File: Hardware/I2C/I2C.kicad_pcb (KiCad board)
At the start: 2 copper layers, 39.4 x 29.2 mm, 5 parts, among them P1 DIL16, P2 CONN_01X04

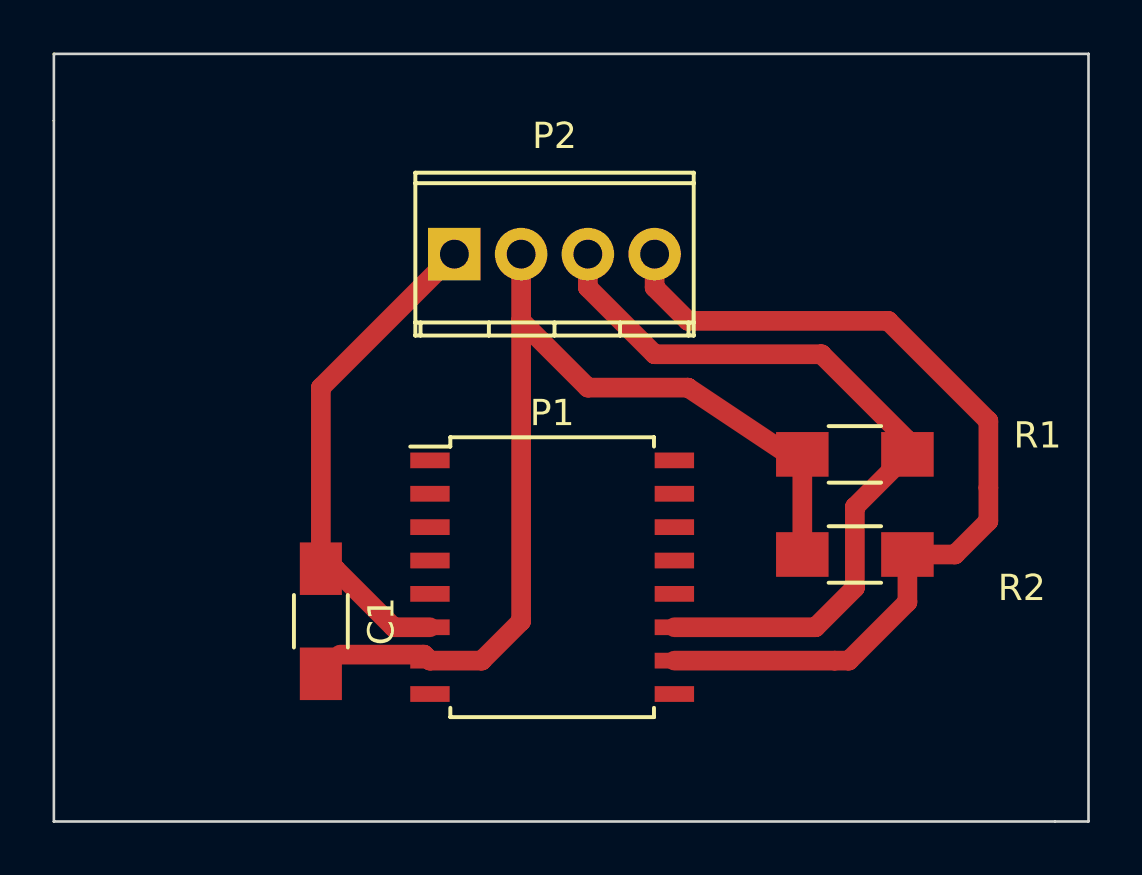
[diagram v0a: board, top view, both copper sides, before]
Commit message: updated I2C design, added various exports used in testing with cnc machine
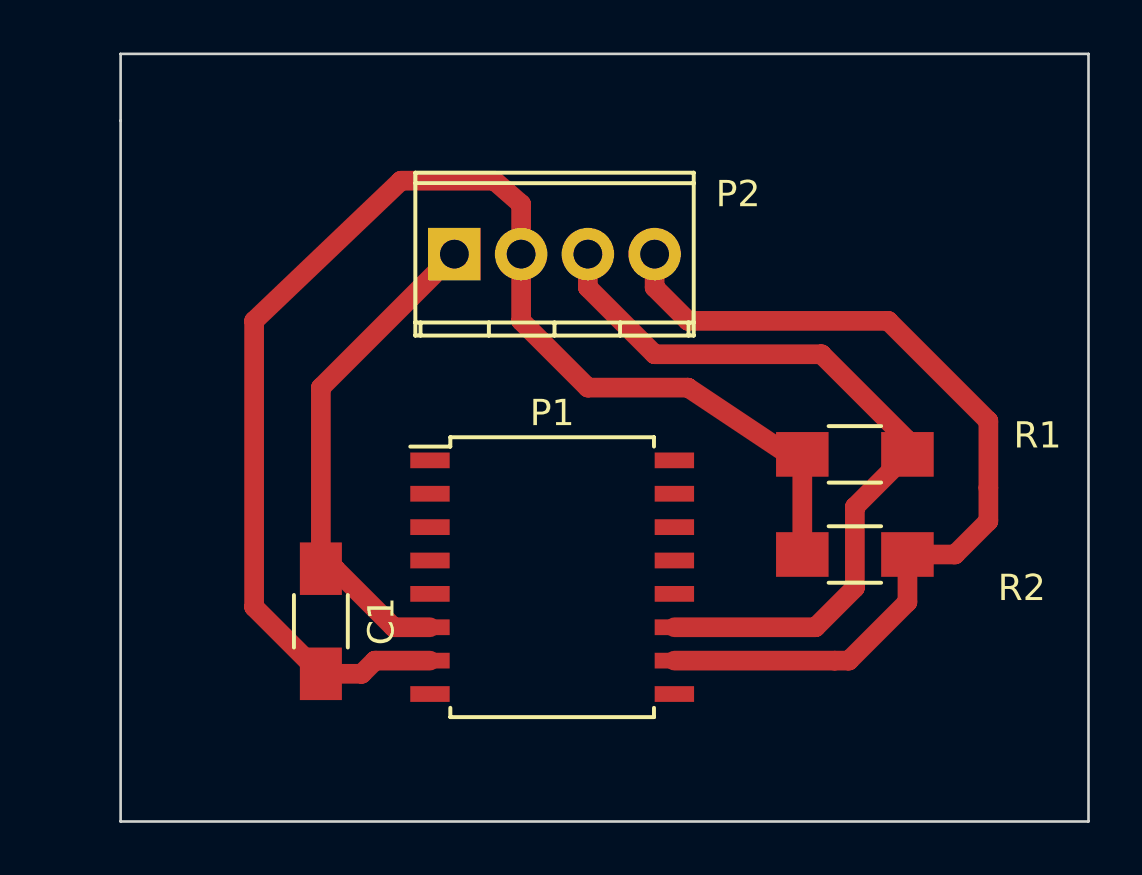
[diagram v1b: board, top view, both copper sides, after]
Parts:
- P1: value DIL16 -> SM9541
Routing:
- net Net-(C1-Pad2): track 37.9 -> 52.2 mm
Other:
- board size 39.4 x 29.2 mm -> 36.8 x 29.2 mm
- board text added: "GND Vs CLK DATA"
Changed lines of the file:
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@@
     (links 10)
     (no_connects 0)
-    (area 129.489999 85.039999 169.063198 114.350001)
+    (area 132.029999 85.039999 169.063198 114.350001)
     (thickness 1.6)
     (drawings 10)
-    (tracks 37)
+    (tracks 41)
     (zones 0)
     (modules 5)
@@
   )
   (setup
-    (last_trace_width 0.75)
+    (last_trace_width 0.25)
     (user_trace_width 0.75)
     (trace_clearance 0.2)
@@
     (pad_to_mask_clearance 0)
     (aux_axis_origin 0 0)
-    (visible_elements FFFFFF7F)
+    (visible_elements 7FFFFFFF)
     (pcbplotparams
-      (layerselection 0x00030_80000001)
+      (layerselection 0x00000_80000000)
       (usegerberextensions false)
       (excludeedgelayer true)
@@
       (padsonsilk false)
       (subtractmaskfromsilk false)
-      (outputformat 1)
+      (outputformat 5)
       (mirror false)
-      (drillshape 1)
+      (drillshape 0)
       (scaleselection 1)
       (outputdirectory ""))
@@
       (effects (font (size 1 1) (thickness 0.15)))
     )
-    (fp_text value DIL16 (at 0 6.25) (layer F.Fab)
+    (fp_text value SM9541 (at 0 6.25) (layer F.Fab)
       (effects (font (size 1 1) (thickness 0.15)))
     )
@@
     (at 144.78 92.71)
     (descr "4-way 2.54mm pitch terminal block, Phoenix MPT series")
-    (fp_text reference P2 (at 3.81 -4.50088) (layer F.SilkS)
+    (fp_text reference P2 (at 10.795 -2.286) (layer F.SilkS)
       (effects (font (size 1 1) (thickness 0.15)))
     )
@@
     )
   )
-  (gr_line (start 168.91 85.09) (end 129.54 85.09) (angle 90) (layer Edge.Cuts) (width 0.1))
-  (gr_line (start 168.91 114.3) (end 167.64 114.3) (angle 90) (layer Edge.Cuts) (width 0.1))
-  (gr_line (start 167.64 114.3) (end 129.54 114.3) (angle 90) (layer Edge.Cuts) (width 0.1))
-  (target plus (at 133.35 88.9) (size 5) (width 0.1) (layer Edge.Cuts))
+  (gr_line (start 132.08 85.09) (end 168.91 85.09) (angle 90) (layer Edge.Cuts) (width 0.1))
+  (gr_line (start 168.91 114.3) (end 132.08 114.3) (angle 90) (layer Edge.Cuts) (width 0.1))
+  (gr_text "GND Vs CLK DATA" (at 148.7805 88.519) (layer F.Mask)
+    (effects (font (size 1 1) (thickness 0.1)))
+  )
+  (target plus (at 135.636 88.9) (size 5) (width 0.1) (layer Edge.Cuts))
   (target plus (at 165.1 110.49) (size 5) (width 0.1) (layer Edge.Cuts))
   (target plus (at 165.1 88.9) (size 5) (width 0.1) (layer Edge.Cuts))
-  (target plus (at 133.35 110.49) (size 5) (width 0.1) (layer Edge.Cuts))
-  (gr_line (start 129.54 85.09) (end 129.54 87.63) (angle 90) (layer Edge.Cuts) (width 0.1))
+  (target plus (at 135.636 110.236) (size 5) (width 0.1) (layer Edge.Cuts))
+  (gr_line (start 132.08 85.09) (end 132.08 87.63) (angle 90) (layer Edge.Cuts) (width 0.1))
   (gr_line (start 168.91 114.3) (end 168.91 85.09) (angle 90) (layer Edge.Cuts) (width 0.1))
-  (gr_line (start 129.54 87.63) (end 129.54 114.3) (angle 90) (layer Edge.Cuts) (width 0.1))
+  (gr_line (start 132.08 87.63) (end 132.08 114.3) (angle 90) (layer Edge.Cuts) (width 0.1))
   (segment (start 144.78 92.71) (end 139.7 97.79) (width 0.75) (layer F.Cu) (net 1))
   (segment (start 139.7 97.79) (end 139.7 104.68) (width 0.75) (layer F.Cu) (net 1))
@@
   (segment (start 140.24 104.68) (end 142.4686 106.9086) (width 0.75) (layer F.Cu) (net 1))
   (segment (start 142.4686 106.9086) (end 143.8511 106.9086) (width 0.75) (layer F.Cu) (net 1))
-  (segment (start 143.8511 108.1786) (end 145.8214 108.1786) (width 0.75) (layer F.Cu) (net 2))
-  (segment (start 147.32 106.68) (end 147.32 95.25) (width 0.75) (layer F.Cu) (net 2))
-  (segment (start 145.8214 108.1786) (end 147.32 106.68) (width 0.75) (layer F.Cu) (net 2))
+  (segment (start 139.7 108.68) (end 141.256 108.68) (width 0.75) (layer F.Cu) (net 2))
+  (segment (start 141.7574 108.1786) (end 143.8511 108.1786) (width 0.75) (layer F.Cu) (net 2))
+  (segment (start 141.256 108.68) (end 141.7574 108.1786) (width 0.75) (layer F.Cu) (net 2))
+  (segment (start 147.32 92.71) (end 147.32 90.805) (width 0.75) (layer F.Cu) (net 2))
+  (segment (start 137.16 106.14) (end 139.7 108.68) (width 0.75) (layer F.Cu) (net 2))
+  (segment (start 137.16 95.25) (end 137.16 106.14) (width 0.75) (layer F.Cu) (net 2))
+  (segment (start 142.748 89.916) (end 137.16 95.25) (width 0.75) (layer F.Cu) (net 2))
+  (segment (start 146.304 89.916) (end 142.748 89.916) (width 0.75) (layer F.Cu) (net 2))
+  (segment (start 147.32 90.805) (end 146.304 89.916) (width 0.75) (layer F.Cu) (net 2))
   (segment (start 158.02 100.33) (end 157.48 100.33) (width 0.75) (layer F.Cu) (net 2) (status 30))
   (segment (start 157.48 100.33) (end 153.67 97.79) (width 0.75) (layer F.Cu) (net 2) (status 10))
@@
   (segment (start 147.32 95.25) (end 147.32 92.71) (width 0.75) (layer F.Cu) (net 2))
   (segment (start 158.02 100.33) (end 158.02 104.14) (width 0.75) (layer F.Cu) (net 2) (status 20))
-  (segment (start 140.43 107.95) (end 143.6225 107.95) (width 0.75) (layer F.Cu) (net 2))
-  (segment (start 143.6225 107.95) (end 143.8511 108.1786) (width 0.75) (layer F.Cu) (net 2))
   (segment (start 159.2514 108.1786) (end 159.7914 108.1786) (width 0.75) (layer F.Cu) (net 10))
   (segment (start 153.1511 108.1786) (end 159.2514 108.1786) (width 0.75) (layer F.Cu) (net 10))
